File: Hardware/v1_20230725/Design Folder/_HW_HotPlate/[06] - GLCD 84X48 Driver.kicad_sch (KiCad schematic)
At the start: 10 parts, among them J601 RCPT_8POS_2ROW_2.54MM_RA

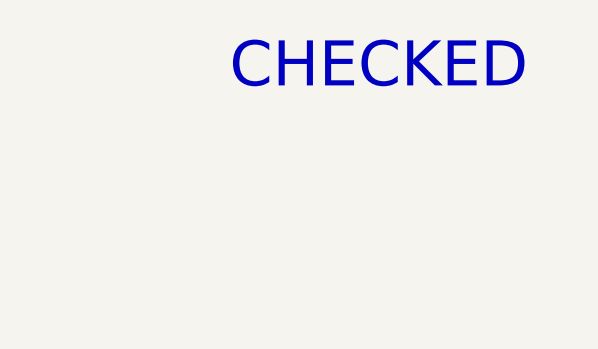
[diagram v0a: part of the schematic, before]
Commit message: Schematic library has been updated
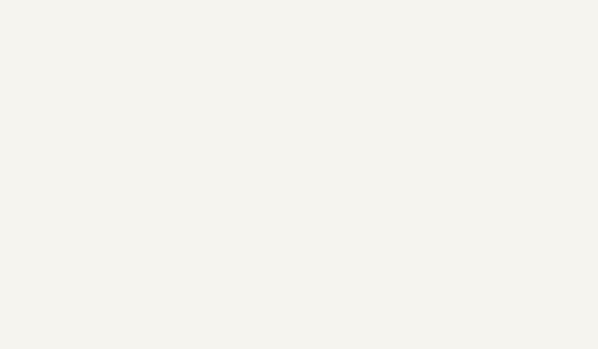
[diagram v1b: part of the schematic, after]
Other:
- note removed: "CHECKED"
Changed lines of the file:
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@@
 (kicad_sch (version 20230121) (generator eeschema)
-  (paper "B")
+  (paper "C")
   (title_block
     (title "Hot Plate")
@@
     (company "Mend0z0")
     (comment 1 "v1")
+    (comment 2 "RELEASED")
     (comment 3 "Siavash Taher Parvar")
     (comment 8 "N/A")
@@
     (stroke (width 0) (type default))
   )
-  (text "CHECKED" (at 382.27 36.83 0)
-    (effects (font (size 5 5)) (justify left bottom))
-  )
   (text "I = 100mA @ +3V3DC" (at 259.08 127 0)

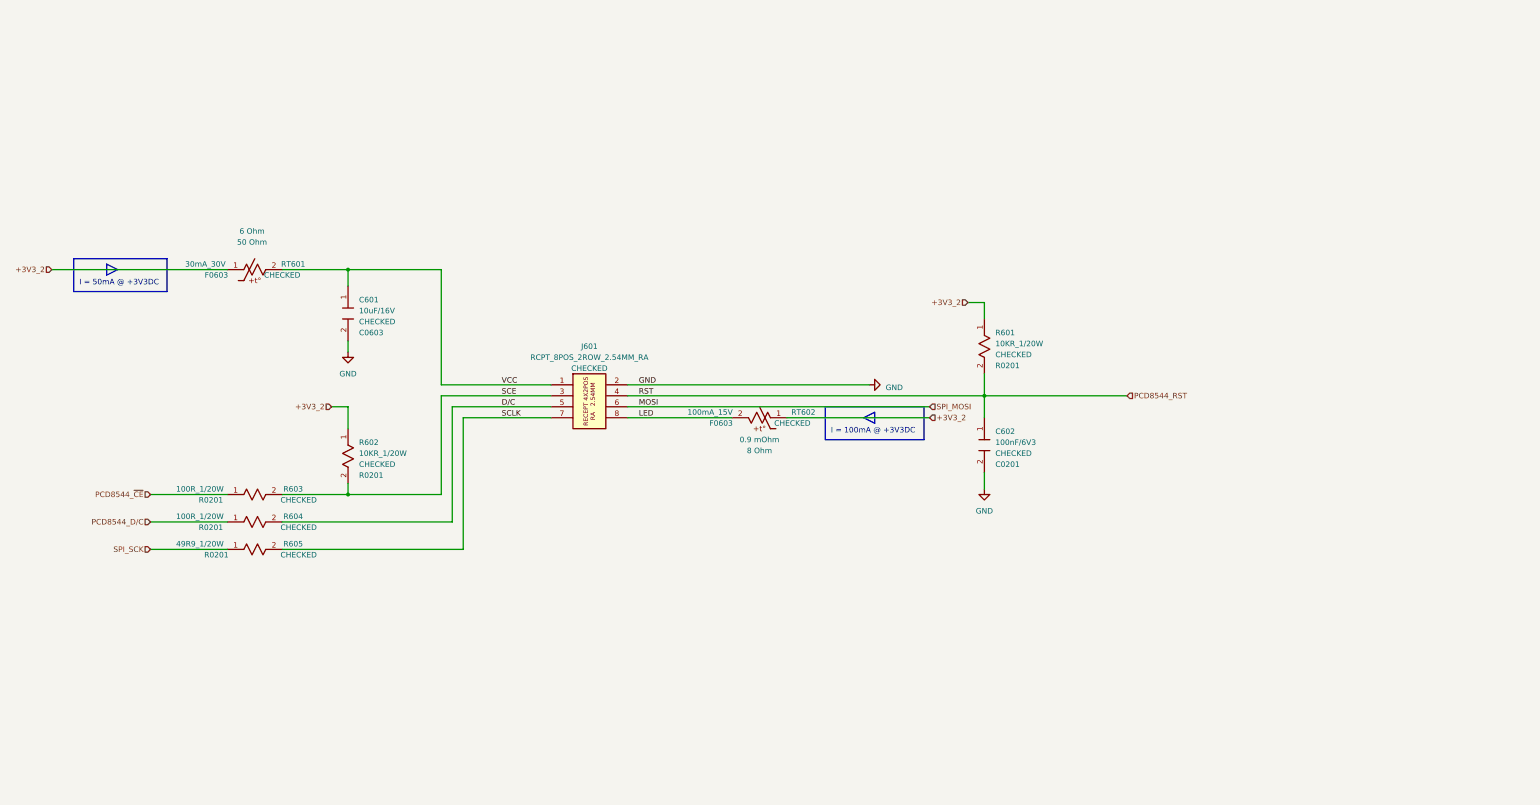
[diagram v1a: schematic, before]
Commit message: components have been updated
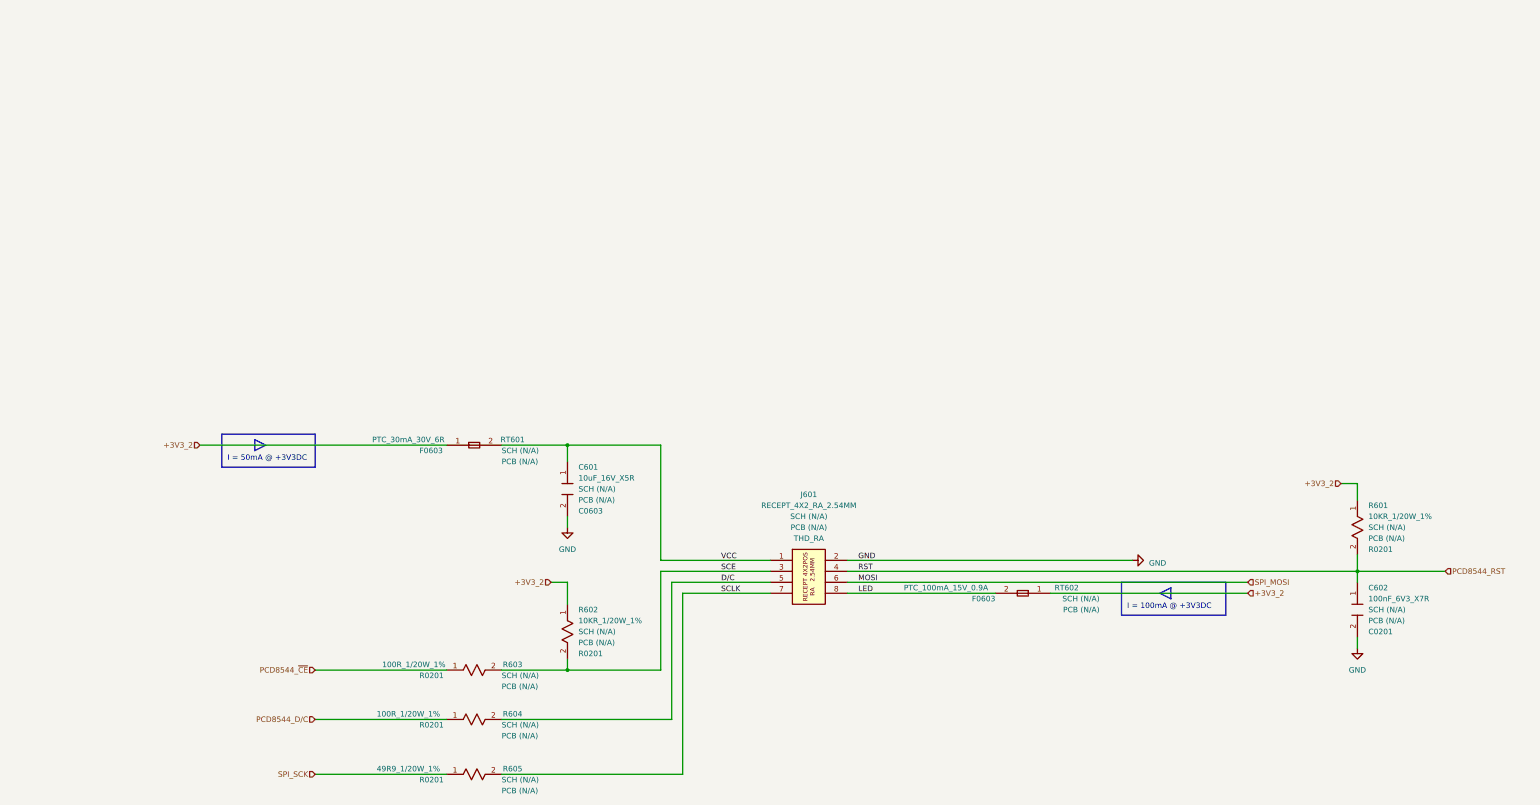
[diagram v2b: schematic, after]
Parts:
- C601: value 10uF/16V -> 10uF_16V_X5R; symbol _SCHLIB_HotPlate:CAP_10uF/16V-C0603 -> _SCHLIB_HotPlate:CAP_10uF_16V_X5R_C0603; Manufacturer (none) -> Murata Electronics; PCB CHECk (none) -> PCB (N/A); Part Number GRT188R61C106KE13J -> (none); Part Number (Manufacturer) (none) -> GRT188R61C106KE13J; Part Number (Vendor) (none) -> 490-GRT188R61C106KE13JTR-ND; SCH CHECK CHECKED -> SCH (N/A); Vendor (none) -> Digikey
- C602: value 100nF/6V3 -> 100nF_6V3_X7R; symbol _SCHLIB_HotPlate:CAP_100nF/6V3_C0201 -> _SCHLIB_HotPlate:CAP_100nF_6V3_X7R_C0201; Manufacturer (none) -> YAGEO; PCB CHECk (none) -> PCB (N/A); Part Number CC0201KRX7R5BB104 -> (none); Part Number (Manufacturer) (none) -> CC0201KRX7R5BB104; Part Number (Vendor) (none) -> 13-CC0201KRX7R5BB104TR-ND; SCH CHECK CHECKED -> SCH (N/A); Vendor (none) -> Digikey
- J601: value RCPT_8POS_2ROW_2.54MM_RA -> RECEPT_4X2_RA_2.54MM; symbol _SCHLIB_HotPlate:CONN_RCPT_8POS_2ROW_2.54MM_RA -> _SCHLIB_HotPlate:CONN_RECEPT_4POS_2ROW_RA_2.54MM; Manufacturer (none) -> Sullins Connector Solutions; PCB CHECk (none) -> PCB (N/A); Package (none) -> THD_RA; Part Number PPTC042LJBN-RC -> (none); Part Number (Manufacturer) (none) -> PPTC042LJBN-RC; Part Number (Vendor) (none) -> S5518-ND; SCH CHECK CHECKED -> SCH (N/A); Vendor (none) -> Digikey
- R601, R602: value 10KR_1/20W -> 10KR_1/20W_1%; symbol _SCHLIB_HotPlate:RES_10KR_1/20W-R0201 -> _SCHLIB_HotPlate:RES_10KR_1/20W_1%_R0201; Manufacturer (none) -> Stackpole Electronics Inc; PCB CHECk (none) -> PCB (N/A); Part Number RMCF0201FT10K0 -> (none); Part Number (Manufacturer) (none) -> RMCF0201FT10K0; Part Number (Vendor) (none) -> RMCF0201FT10K0TR-ND; SCH CHECK CHECKED -> SCH (N/A); Vendor (none) -> Digikey
- R603, R604: value 100R_1/20W -> 100R_1/20W_1%; symbol _SCHLIB_HotPlate:RES_100R_1/20W-R0201 -> _SCHLIB_HotPlate:RES_100R_1/20W_1%_R0201; Manufacturer (none) -> Stackpole Electronics Inc; PCB CHECk (none) -> PCB (N/A); Part Number RMCF0201FT100R -> (none); Part Number (Manufacturer) (none) -> RMCF0201FT100R; Part Number (Vendor) (none) -> RMCF0201FT100RTR-ND; SCH CHECK CHECKED -> SCH (N/A); Vendor (none) -> Digikey
- R605: value 49R9_1/20W -> 49R9_1/20W_1%; symbol _SCHLIB_HotPlate:RES_49R9_1/20W-R0201 -> _SCHLIB_HotPlate:RES_49R9_1/20W_1%_R0201; Manufacturer (none) -> Stackpole Electronics Inc; PCB CHECk (none) -> PCB (N/A); Part Number RMCF0201FT49R9 -> (none); Part Number (Manufacturer) (none) -> RMCF0201FT49R9; Part Number (Vendor) (none) -> RMCF0201FT49R9TR-ND; SCH CHECK CHECKED -> SCH (N/A); Vendor (none) -> Digikey
- RT601: value 30mA_30V -> PTC_30mA_30V_6R; symbol _SCHLIB_HotPlate:PTC_0ZCM0003FF2G_F0603 -> _SCHLIB_HotPlate:FUSE_PTC_0ZCM0003FF2G_0.03A_0.09A_6R_F0603; Init resistance 6 Ohm -> (none); Manufacturer (none) -> Bel Fuse Inc.; PCB CHECk (none) -> PCB (N/A); Part Number 0ZCM0003FF2G -> (none); Part Number (Manufacturer) (none) -> 0ZCM0003FF2G; Part Number (Vendor) (none) -> 507-0ZCM0003FF2GTR-ND; Post trip resistance 50 Ohm -> (none); SCH CHECK CHECKED -> SCH (N/A); Vendor (none) -> Digikey
- RT602: value 100mA_15V -> PTC_100mA_15V_0.9A; symbol _SCHLIB_HotPlate:PTC_0ZCM0010FF2G_F0603 -> _SCHLIB_HotPlate:FUSE_PTC_0ZCM0010FF2G_0.1A_0.25A_15V_0.9A_F0603; Init resistance 0.9 mOhm -> (none); Manufacturer (none) -> Bel Fuse Inc.; PCB CHECk (none) -> PCB (N/A); Part Number 0ZCM0010FF2G -> (none); Part Number (Manufacturer) (none) -> 0ZCM0010FF2G; Part Number (Vendor) (none) -> 507-1818-2-ND; Post trip resistance 8 Ohm -> (none); SCH CHECK CHECKED -> SCH (N/A); Vendor (none) -> Digikey
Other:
- moved on the sheet: C601, C602, J601, R601, R602, R603, R604, R605
